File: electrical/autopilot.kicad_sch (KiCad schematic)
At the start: 4 parts

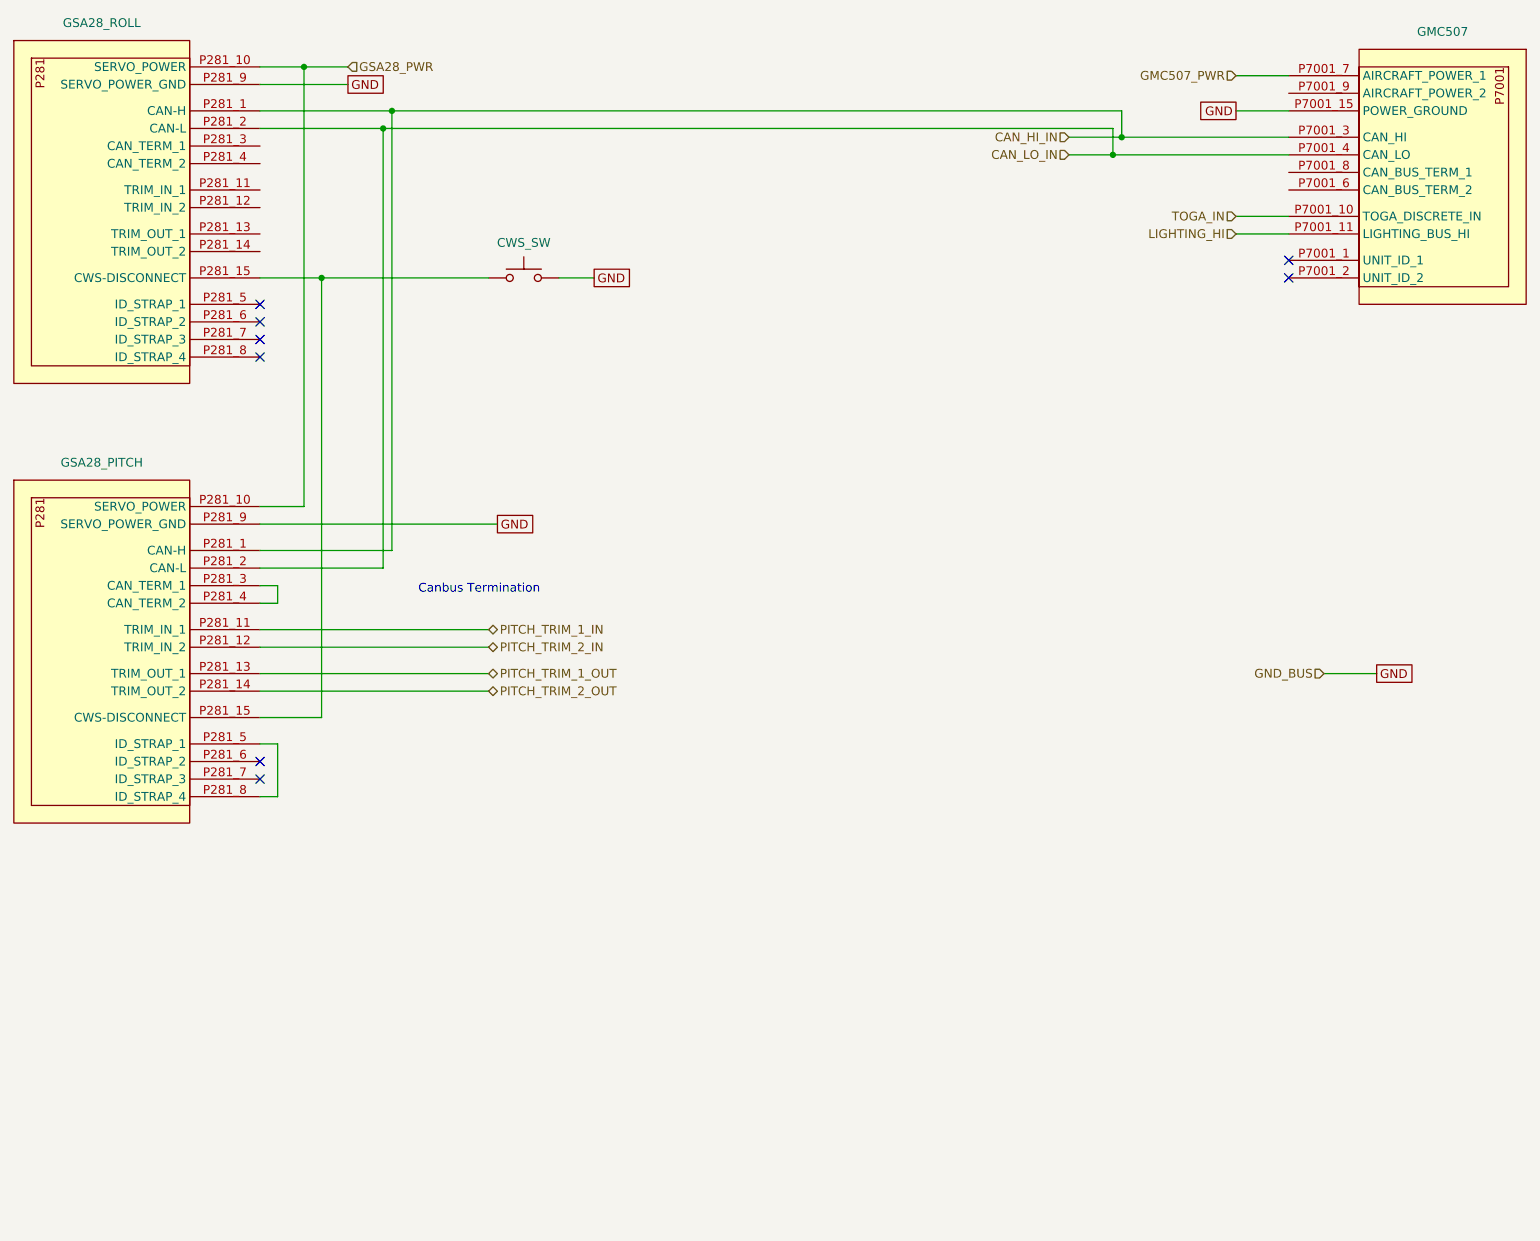
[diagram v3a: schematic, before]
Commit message: Updated electrical to not use IBBS. Also, added BT adapter and 3P3T switch.
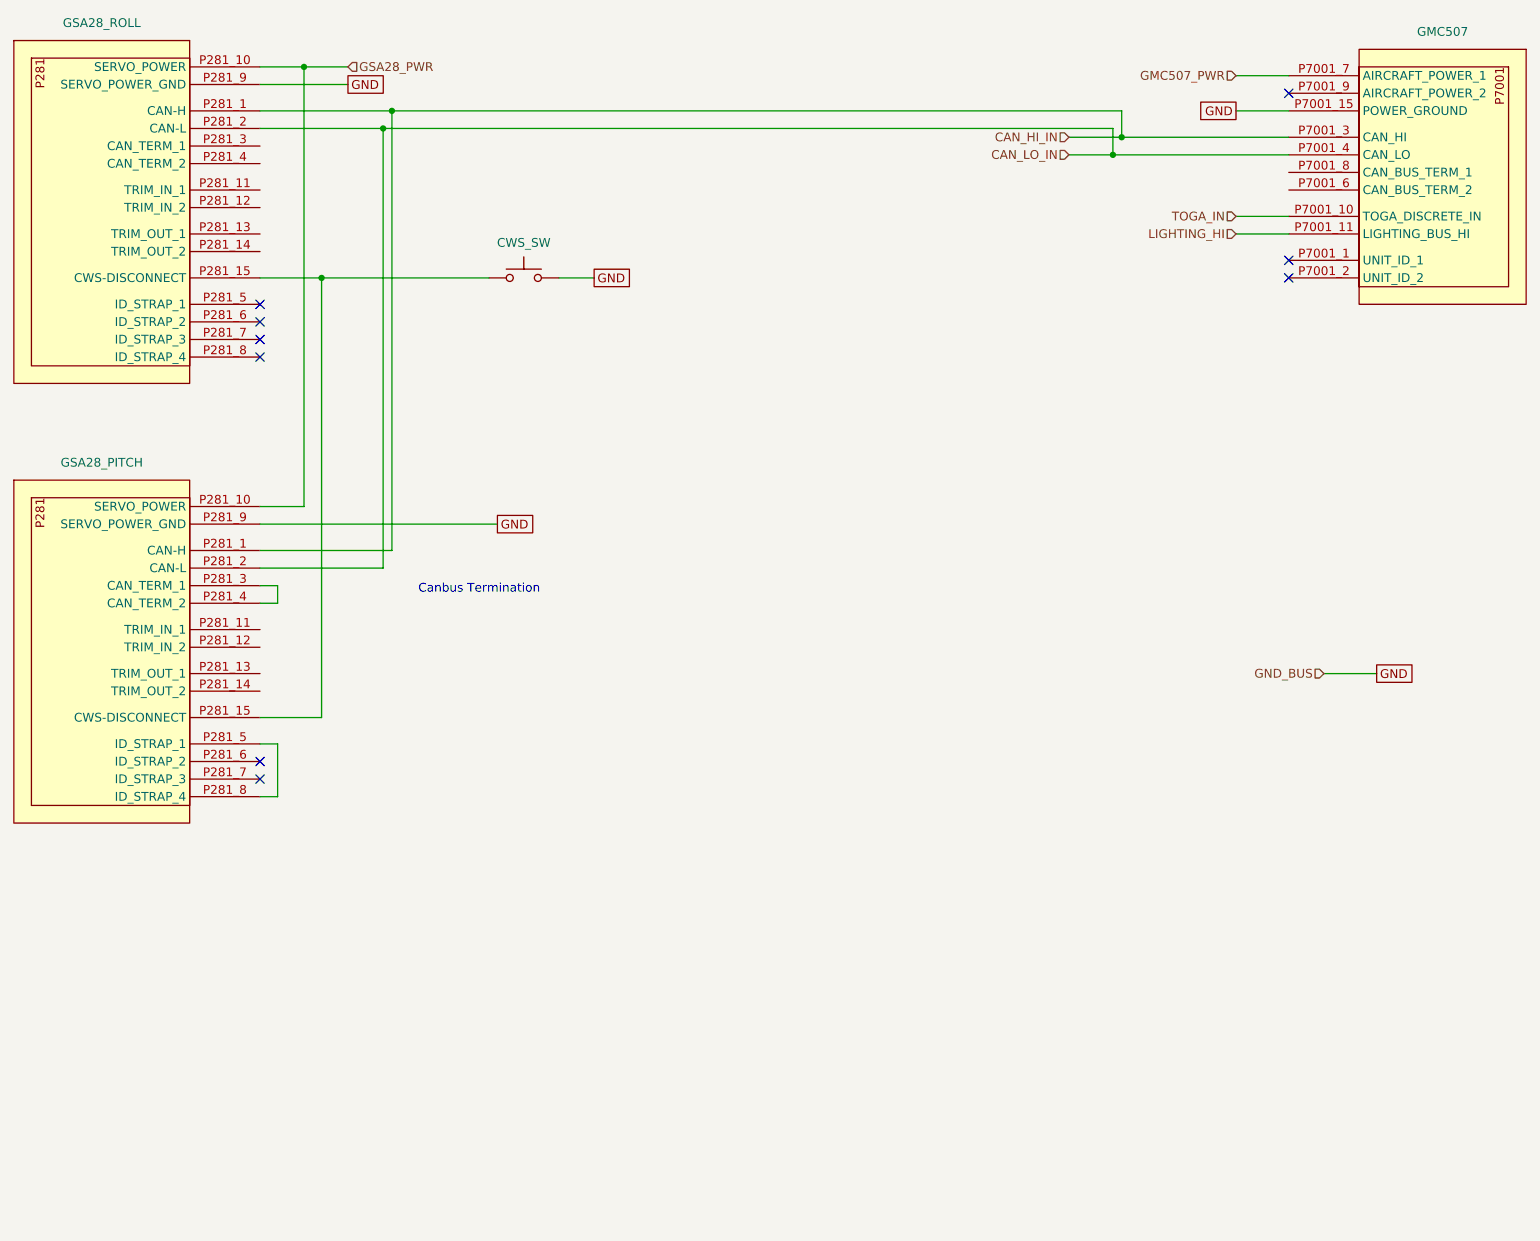
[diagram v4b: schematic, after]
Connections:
- net PITCH_TRIM_1_IN: no longer names the net of GSA28_PITCH.P281_11 (TRIM_IN_1)
- net PITCH_TRIM_1_OUT: no longer names the net of GSA28_PITCH.P281_13 (TRIM_OUT_1)
- net PITCH_TRIM_2_IN: no longer names the net of GSA28_PITCH.P281_12 (TRIM_IN_2)
- net PITCH_TRIM_2_OUT: no longer names the net of GSA28_PITCH.P281_14 (TRIM_OUT_2)
- no-connect marks 8 -> 9
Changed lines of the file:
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@@
   (no_connect (at 55.88 57.15))
   (no_connect (at 55.88 125.73))
+  (no_connect (at 204.47 26.67))
   (wire (pts (xy 55.88 95.25) (xy 73.66 95.25))
-    (stroke (width 0) (type default))
-  )
-  (wire (pts (xy 55.88 106.68) (xy 88.9 106.68))
     (stroke (width 0) (type default))
   )
@@
     (stroke (width 0) (type default))
   )
-  (wire (pts (xy 55.88 104.14) (xy 88.9 104.14))
+  (wire (pts (xy 196.85 44.45) (xy 204.47 44.45))
     (stroke (width 0) (type default))
   )
@@
   )
   (wire (pts (xy 73.66 31.75) (xy 73.66 95.25))
-    (stroke (width 0) (type default))
-  )
-  (wire (pts (xy 55.88 113.03) (xy 88.9 113.03))
     (stroke (width 0) (type default))
   )
@@
     (stroke (width 0) (type default))
   )
-  (wire (pts (xy 55.88 110.49) (xy 88.9 110.49))
-    (stroke (width 0) (type default))
-  )
   (wire (pts (xy 64.77 53.34) (xy 88.9 53.34))
     (stroke (width 0) (type default))
   )
   (wire (pts (xy 209.55 110.49) (xy 217.17 110.49))
-    (stroke (width 0) (type default))
-  )
-  (wire (pts (xy 196.85 44.45) (xy 204.47 44.45))
     (stroke (width 0) (type default))
   )
@@
     (effects (font (size 1.27 1.27)) (justify right))
   )
+  (hierarchical_label "TOGA_IN" (shape input) (at 196.85 44.45 180) (fields_autoplaced)
+    (effects (font (size 1.27 1.27)) (justify right))
+  )
   (hierarchical_label "GMC507_PWR" (shape input) (at 196.85 24.13 180) (fields_autoplaced)
     (effects (font (size 1.27 1.27)) (justify right))
@@
     (effects (font (size 1.27 1.27)) (justify left))
   )
-  (hierarchical_label "PITCH_TRIM_1_IN" (shape bidirectional) (at 88.9 104.14 0) (fields_autoplaced)
-    (effects (font (size 1.27 1.27)) (justify left))
-  )
   (hierarchical_label "CAN_LO_IN" (shape input) (at 172.72 35.56 180) (fields_autoplaced)
     (effects (font (size 1.27 1.27)) (justify right))
   )
-  (hierarchical_label "PITCH_TRIM_2_IN" (shape bidirectional) (at 88.9 106.68 0) (fields_autoplaced)
-    (effects (font (size 1.27 1.27)) (justify left))
-  )
-  (hierarchical_label "TOGA_IN" (shape input) (at 196.85 44.45 180) (fields_autoplaced)
-    (effects (font (size 1.27 1.27)) (justify right))
-  )
-  (hierarchical_label "PITCH_TRIM_1_OUT" (shape bidirectional) (at 88.9 110.49 0) (fields_autoplaced)
-    (effects (font (size 1.27 1.27)) (justify left))
-  )
-  (hierarchical_label "PITCH_TRIM_2_OUT" (shape bidirectional) (at 88.9 113.03 0) (fields_autoplaced)
-    (effects (font (size 1.27 1.27)) (justify left))
-  )
   (hierarchical_label "GND_BUS" (shape input) (at 209.55 110.49 180) (fields_autoplaced)

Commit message: Updated canbus diagrams with order for where magnometer and servos will be located. Added yaw servo.
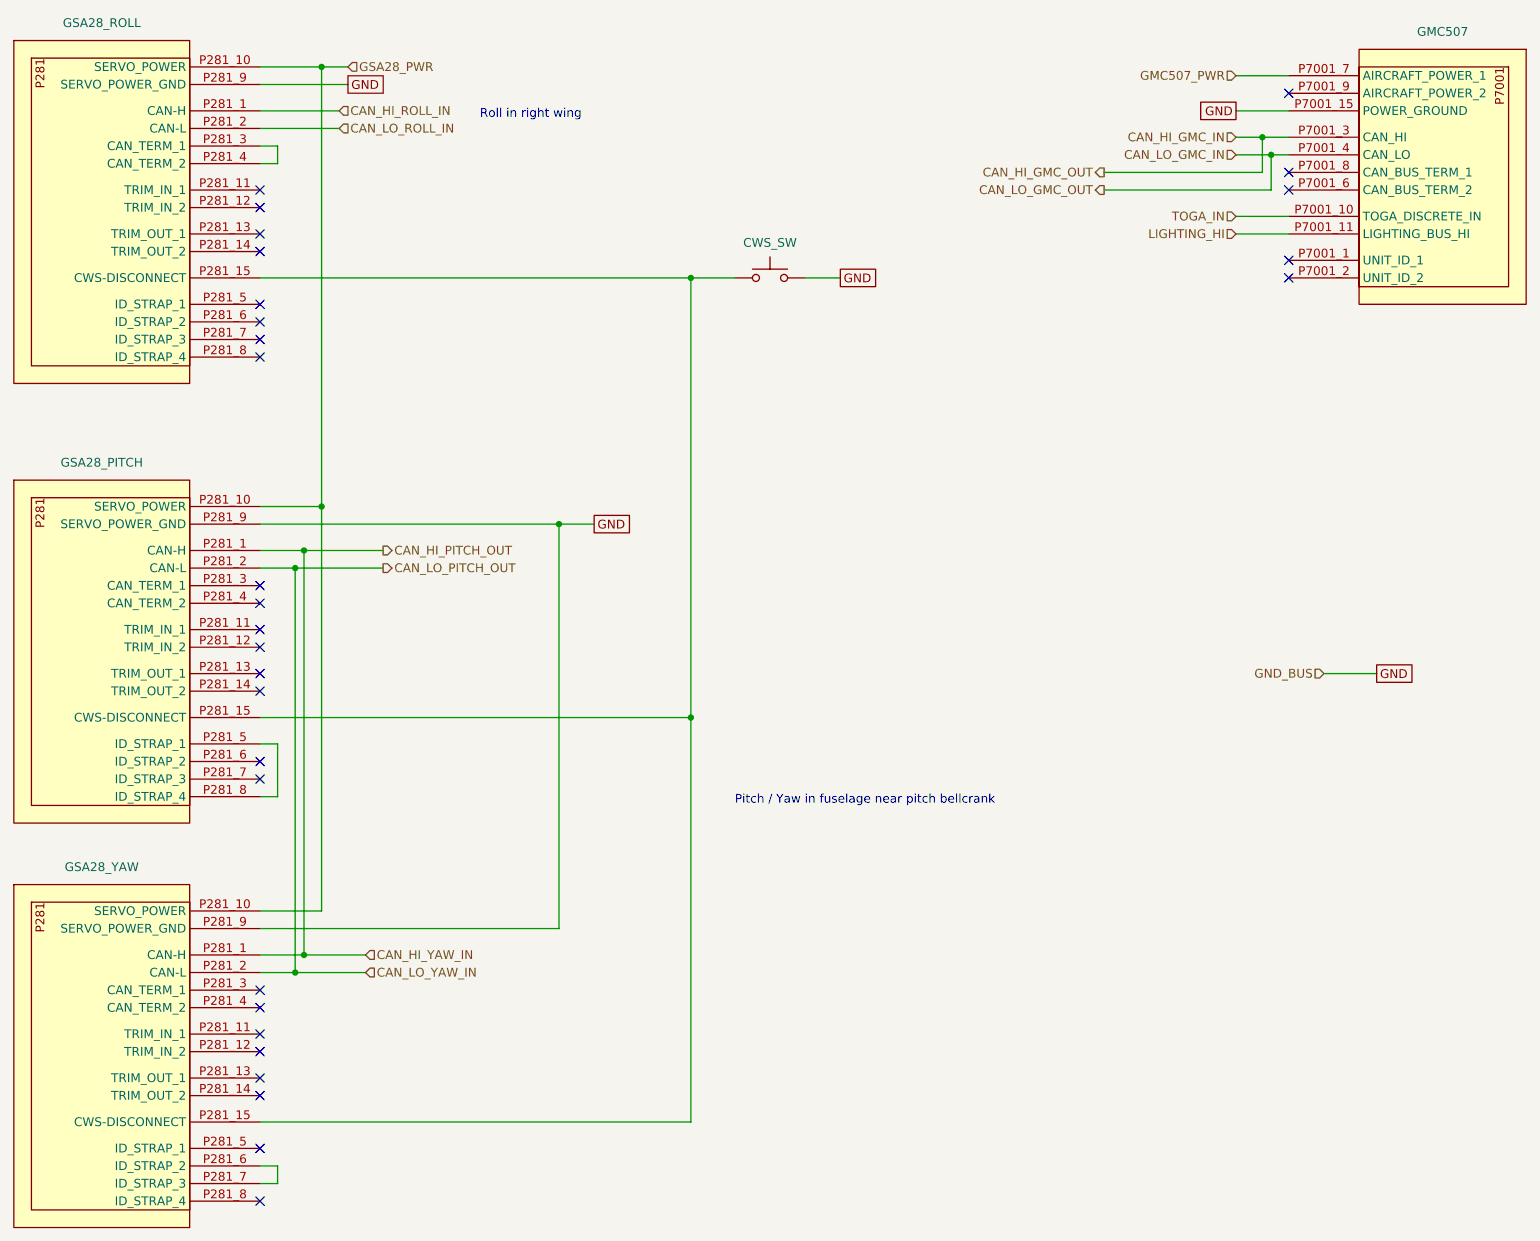
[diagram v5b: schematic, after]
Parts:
- added GSA28_YAW: ~, symbol flyerx:Garmin_GSA28
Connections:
- net GND: now also GSA28_YAW.P281_9 (SERVO_POWER_GND)
- net GSA28_PWR: now also GSA28_YAW.P281_10 (SERVO_POWER)
- net at CWS_SW.1, GSA28_PITCH.P281_15 (CWS-DISCONNECT), GSA28_ROLL.P281_15 (CWS-DISCONNECT): now also GSA28_YAW.P281_15 (CWS-DISCONNECT)
- net at GSA28_ROLL.P281_3 (CAN_TERM_1): now also GSA28_ROLL.P281_4 (CAN_TERM_2)
- net at GSA28_PITCH.P281_3 (CAN_TERM_1): no longer GSA28_PITCH.P281_4 (CAN_TERM_2)
- removed net CAN_HI_IN: GMC507.P7001_3 (CAN_HI), GSA28_PITCH.P281_1 (CAN-H), GSA28_ROLL.P281_1 (CAN-H)
- removed net CAN_LO_IN: GMC507.P7001_4 (CAN_LO), GSA28_PITCH.P281_2 (CAN-L), GSA28_ROLL.P281_2 (CAN-L)
- new net: GSA28_YAW.P281_6 (ID_STRAP_2), GSA28_YAW.P281_7 (ID_STRAP_3)
- new net CAN_HI_GMC_IN: GMC507.P7001_3 (CAN_HI)
- new net CAN_HI_PITCH_OUT: GSA28_PITCH.P281_1 (CAN-H), GSA28_YAW.P281_1 (CAN-H)
- new net CAN_HI_ROLL_IN: GSA28_ROLL.P281_1 (CAN-H)
- new net CAN_LO_GMC_IN: GMC507.P7001_4 (CAN_LO)
- new net CAN_LO_PITCH_OUT: GSA28_PITCH.P281_2 (CAN-L), GSA28_YAW.P281_2 (CAN-L)
- new net CAN_LO_ROLL_IN: GSA28_ROLL.P281_2 (CAN-L)
- no-connect marks 9 -> 29
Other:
- note added: "Pitch / Yaw in fuselage near pitch bellcrank"
- note added: "Roll in right wing"
- note removed: "Canbus Termination"
- moved on the sheet: CWS_SW
